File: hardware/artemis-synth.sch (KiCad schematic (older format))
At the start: 41 parts, among them IC1 ATMEGA328P, J1 AVR-ISP-6, J2 CONN JACK STEREO R/A 3PIN 3.5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, SW1 SWITCH_PUSH_CW, SW10 SWITCH_PUSH_CW, SW2 SWITCH_PUSH_CW, SW3 SWITCH_PUSH_CW, SW4 SWITCH_PUSH_CW, SW5 SWITCH_PUSH_CW, SW6 SWITCH_PUSH_CW, SW7 SWITCH_PUSH_CW, SW8 SWITCH_PUSH_CW, SW9 SWITCH_PUSH_CW, U1 MCP4921

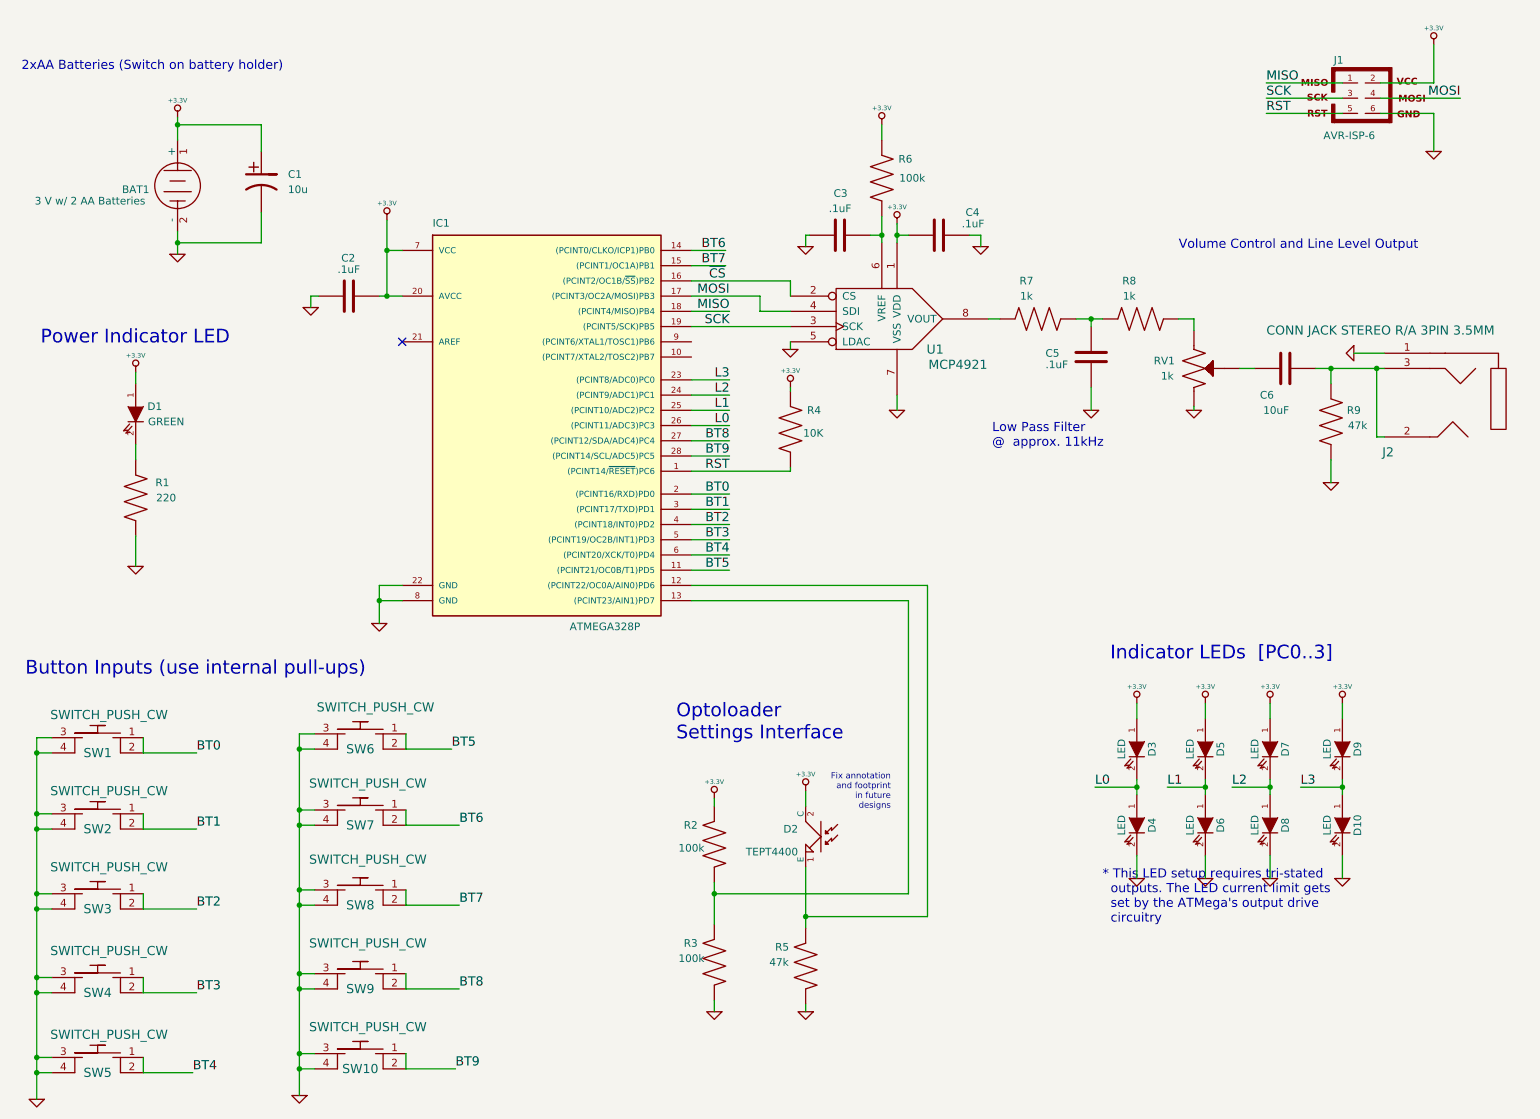
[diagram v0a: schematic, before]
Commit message: Generated latest gerber files for the v2rC board. Should be the final changes before getting sent out. Cleared todo list, plotted latest pdf of schematic. Changed output stage to add a pot which approximates a log pot (using R8). Changed C6 to move lower frequency pole up to 2Hz from .1Hz. Moved HF pole to about 5kHz to fit the new output samplign rate of 11kHz. Ideally we can mvoe back to 22kHz with some firmware optimization. THe new output stage is also boosted from its previous form in v2rB so that it can drive headphones pretty loudly.
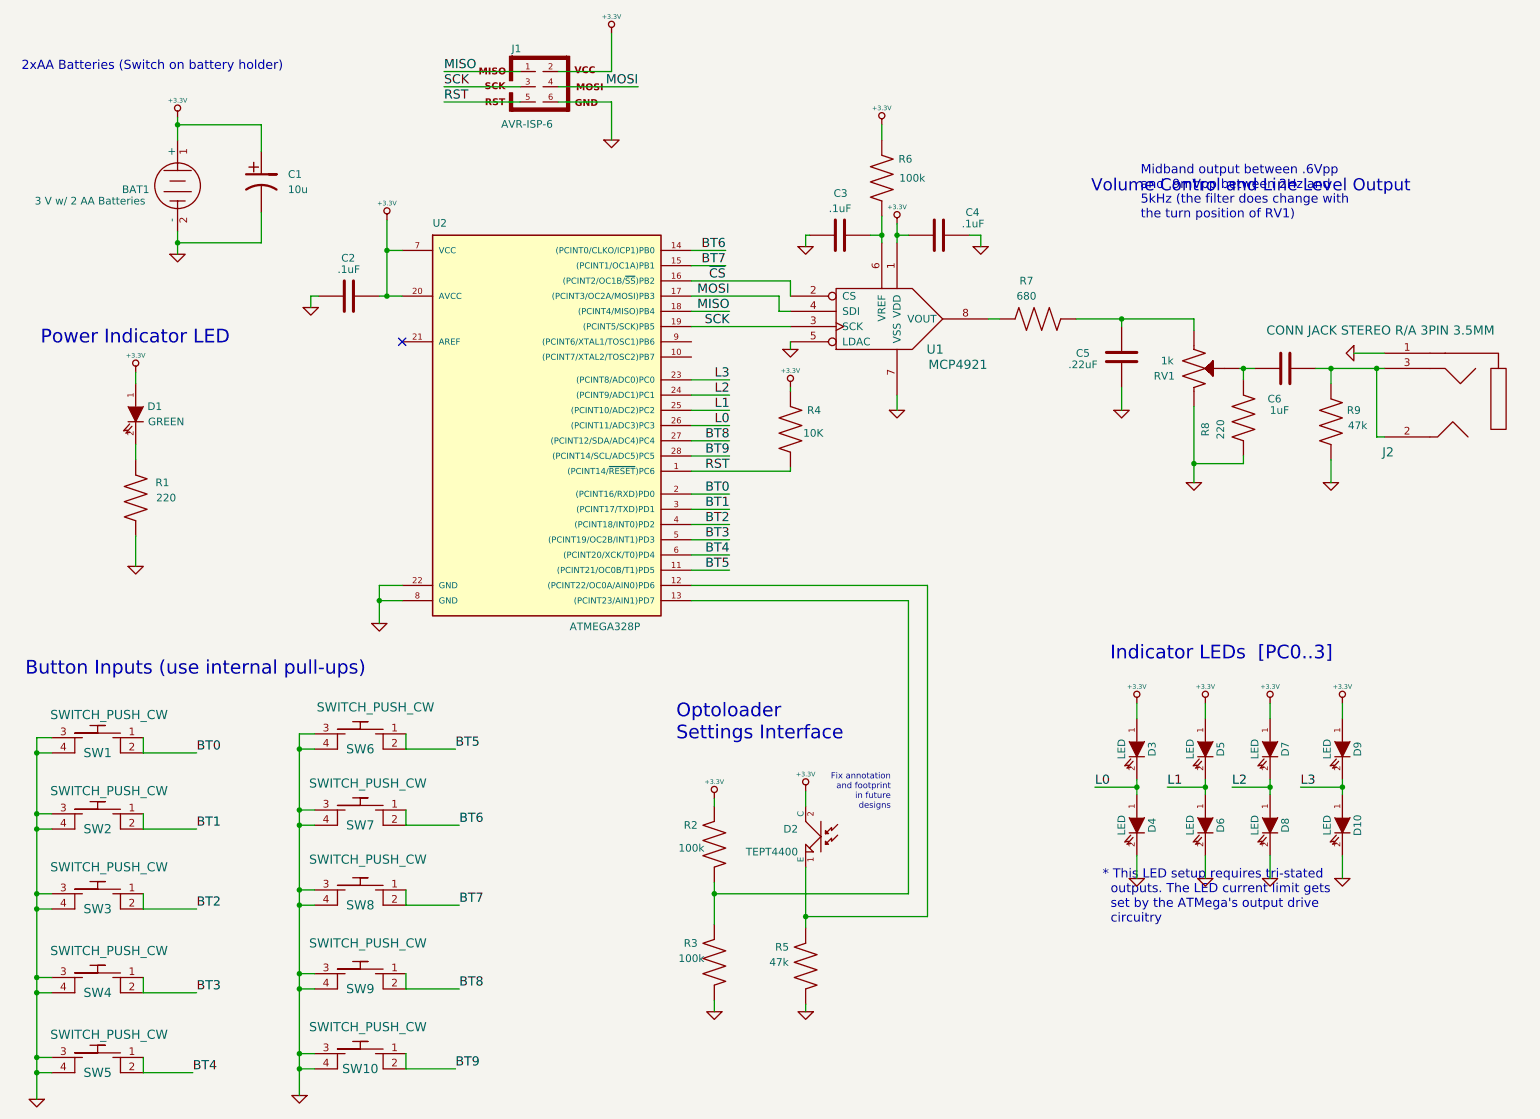
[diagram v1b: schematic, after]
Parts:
- C5: value .1uF -> .22uF
- C6: value 10uF -> 1uF; footprint C1V8 -> C1
- D1, D10, D2, D3, D4, D5, D6, D7, D8, D9: footprint LED-3MM -> LED-3MM-CORRECTED
- R7: value 1k -> 680
- R8: value 1k -> 220
- renumbered IC1 to U2
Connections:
- net GND: now also R8.1, RV1.1; no longer RV1.3
- net at C5.1, R7.2: now also RV1.3; no longer R8.1
- net at R8.2: now also C6.1, RV1.2; no longer RV1.1
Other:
- note added: "Midband output between .6Vpp \nand .9mVpp between 2Hz and \n5kHz (the filter does change with \nthe turn position of RV1)"
- note removed: "Low Pass Filter \n@ approx. 11kHz\n"
- moved on the sheet: C5, J1
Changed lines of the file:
@@
-EESchema Schematic File Version 2  date Tue 09 Jul 2013 12:50:36 PM EDT
+EESchema Schematic File Version 2  date Thu 11 Jul 2013 01:59:12 PM EDT
 LIBS:power
 LIBS:device
@@
 Sheet 1 1
 Title "Artemis Synthesizer"
-Date "9 jul 2013"
+Date "11 jul 2013"
 Rev "C"
 Comp "Christopher Woodall (c) 2012-2013"
@@
 F 0 "D4" H 8025 5950 50  0000 C CNN
 F 1 "LED" H 8025 5750 50  0000 C CNN
-F 2 "LED-3MM" H 8025 5850 50  0001 C CNN
+F 2 "LED-3MM-CORRECTED" H 8025 5850 50  0001 C CNN
 	1    8025 5850
 	0    1    1    0
@@
 F 0 "D6" H 8475 5950 50  0000 C CNN
 F 1 "LED" H 8475 5750 50  0000 C CNN
-F 2 "LED-3MM" H 8475 5850 50  0001 C CNN
+F 2 "LED-3MM-CORRECTED" H 8475 5850 50  0001 C CNN
 	1    8475 5850
 	0    1    1    0
@@
 F 0 "D8" H 8900 5950 50  0000 C CNN
 F 1 "LED" H 8900 5750 50  0000 C CNN
-F 2 "LED-3MM" H 8900 5850 50  0001 C CNN
+F 2 "LED-3MM-CORRECTED" H 8900 5850 50  0001 C CNN
 	1    8900 5850
 	0    1    1    0
@@
 F 0 "D10" H 9375 5950 50  0000 C CNN
 F 1 "LED" H 9375 5750 50  0000 C CNN
-F 2 "LED-3MM" H 9375 5850 50  0001 C CNN
+F 2 "LED-3MM-CORRECTED" H 9375 5850 50  0001 C CNN
 	1    9375 5850
 	0    1    1    0
@@
 F 0 "D9" H 9375 5450 50  0000 C CNN
 F 1 "LED" H 9375 5250 50  0000 C CNN
-F 2 "LED-3MM" H 9375 5350 50  0001 C CNN
+F 2 "LED-3MM-CORRECTED" H 9375 5350 50  0001 C CNN
 	1    9375 5350
 	0    1    1    0
@@
 F 0 "D7" H 8900 5450 50  0000 C CNN
 F 1 "LED" H 8900 5250 50  0000 C CNN
-F 2 "LED-3MM" H 8900 5350 50  0001 C CNN
+F 2 "LED-3MM-CORRECTED" H 8900 5350 50  0001 C CNN
 	1    8900 5350
 	0    1    1    0
@@
 F 0 "D5" H 8475 5450 50  0000 C CNN
 F 1 "LED" H 8475 5250 50  0000 C CNN
-F 2 "LED-3MM" H 8475 5350 50  0001 C CNN
+F 2 "LED-3MM-CORRECTED" H 8475 5350 50  0001 C CNN
 	1    8475 5350
 	0    1    1    0
@@
 F 0 "D3" H 8025 5450 50  0000 C CNN
 F 1 "LED" H 8025 5250 50  0000 C CNN
-F 2 "LED-3MM" H 8025 5350 50  0001 C CNN
+F 2 "LED-3MM-CORRECTED" H 8025 5350 50  0001 C CNN
 	1    8025 5350
 	0    1    1    0
@@
 	-1   0    0    -1
 $EndComp
-Text Label 3525 5350 0    60   ~ 0
+Text Label 3550 5350 0    60   ~ 0
 BT5
 Text Label 3575 5850 0    60   ~ 0
@@
 L +3.3V #PWR017
 U 1 1 4FE8EEAB
-P 9975 725
-F 0 "#PWR017" H 9975 685 30  0001 C CNN
-F 1 "+3.3V" H 9975 835 30  0000 C CNN
-	1    9975 725
+P 4575 650
+F 0 "#PWR017" H 4575 610 30  0001 C CNN
+F 1 "+3.3V" H 4575 760 30  0000 C CNN
+	1    4575 650
 	1    0    0    -1
 $EndComp
@@
 Text Label 5350 2575 2    60   ~ 0
 SCK
-Text Label 8875 1175 0    60   ~ 0
+Text Label 3475 1100 0    60   ~ 0
 RST
-Text Label 8875 1075 0    60   ~ 0
+Text Label 3475 1000 0    60   ~ 0
 SCK
-Text Label 8875 975  0    60   ~ 0
+Text Label 3475 900  0    60   ~ 0
 MISO
-Text Label 10150 1075 2    60   ~ 0
+Text Label 4750 1000 2    60   ~ 0
 MOSI
 $Comp
 L GND #PWR025
 U 1 1 4FDAC48B
-P 9975 1425
-F 0 "#PWR025" H 9975 1425 30  0001 C CNN
-F 1 "GND" H 9975 1355 30  0001 C CNN
-	1    9975 1425
-	1    0    0    -1
-$EndComp
-$Comp
-L ATMEGA328P-P IC1
+P 4575 1350
+F 0 "#PWR025" H 4575 1350 30  0001 C CNN
+F 1 "GND" H 4575 1280 30  0001 C CNN
+	1    4575 1350
+	1    0    0    -1
+$EndComp
+$Comp
+L ATMEGA328P-P U2
 U 1 1 4FDABFE3
 P 4100 3175
-F 0 "IC1" H 3400 4425 50  0000 L BNN
+F 0 "U2" H 3400 4425 50  0000 L BNN
 F 1 "ATMEGA328P" H 4300 1775 50  0000 L BNN
 F 2 "DIP-28__300" H 3500 1825 50  0001 C CNN
@@
 L AVR-ISP-6 J1
 U 1 1 4FDABF46
-P 9500 1075
-F 0 "J1" H 9350 1325 50  0000 C CNN
-F 1 "AVR-ISP-6" H 9250 800 50  0000 L BNN
-F 2 "pin_array_3x2" V 9000 1075 50  0001 C CNN
-	1    9500 1075
+P 4100 1000
+F 0 "J1" H 3950 1250 50  0000 C CNN
+F 1 "AVR-ISP-6" H 3850 725 50  0000 L BNN
+F 2 "pin_array_3x2" V 3600 1000 50  0001 C CNN
+	1    4100 1000
 	1    0    0    -1
 $EndComp
@@
 F 0 "D2" H 6100 5975 50  0000 L CNN
 F 1 "TEPT4400" H 6100 5825 50  0000 L CNN
-F 2 "LED-3MM" H 6100 5925 50  0001 C CNN
+F 2 "LED-3MM-CORRECTED" H 6100 5925 50  0001 C CNN
 	1    5950 5925
 	-1   0    0    -1
@@
 $EndComp
 $Comp
-L R_US R8
-U 1 1 51D3454A
-P 8050 2525
-F 0 "R8" V 8300 2600 50  0000 C CNN
-F 1 "1k" V 8200 2600 50  0000 C CNN
-F 2 "R4" V 8300 2600 50  0001 C CNN
-	1    8050 2525
-	0    -1   -1   0
-$EndComp
-$Comp
 L POT_US RV1
 U 1 1 51D34592
@@
 F 2 "THUMBWHEEL_POT_3352T" H 8225 2900 50  0001 C CNN
 	1    8400 2850
-	1    0    0    -1
+	1    0    0    1
 $EndComp
 $Comp
@@
 P 7375 2525
 F 0 "R7" V 7625 2600 50  0000 C CNN
-F 1 "1k" V 7525 2600 50  0000 C CNN
+F 1 "680" V 7525 2600 50  0000 C CNN
 F 2 "R4" V 7625 2600 50  0001 C CNN
 	1    7375 2525
@@
 L C C5
 U 1 1 51D3459E
-P 7725 2775
-F 0 "C5" H 7425 2800 50  0000 L CNN
-F 1 ".1uF" H 7425 2725 50  0000 L CNN
-F 2 "C1" H 7550 2775 50  0001 C CNN
-	1    7725 2775
+P 7925 2775
+F 0 "C5" H 7625 2800 50  0000 L CNN
+F 1 ".22uF" H 7575 2725 50  0000 L CNN
+F 2 "C1" H 7750 2775 50  0001 C CNN
+	1    7925 2775
 	1    0    0    -1
 $EndComp
@@
 U 1 1 51D345AA
 P 9000 2850
-F 0 "C6" V 8825 2925 50  0000 L CNN
-F 1 "10uF" V 8725 2825 50  0000 L CNN
-F 2 "C1V8" H 8825 2850 50  0001 C CNN
+F 0 "C6" V 8800 2875 50  0000 L CNN
+F 1 "1uF" V 8725 2825 50  0000 L CNN
+F 2 "C1" H 8825 2850 50  0001 C CNN
 	1    9000 2850
 	0    -1   -1   0
@@
 L GND #PWR030
 U 1 1 51D351B9
-P 8400 3125
-F 0 "#PWR030" H 8400 3125 30  0001 C CNN
-F 1 "GND" H 8400 3055 30  0001 C CNN
-	1    8400 3125
+P 8400 3600
+F 0 "#PWR030" H 8400 3600 30  0001 C CNN
+F 1 "GND" H 8400 3530 30  0001 C CNN
+	1    8400 3600
 	1    0    0    -1
 $EndComp
@@
 L GND #PWR031
 U 1 1 51D35725
-P 7725 3125
-F 0 "#PWR031" H 7725 3125 30  0001 C CNN
-F 1 "GND" H 7725 3055 30  0001 C CNN
-	1    7725 3125
+P 7925 3125
+F 0 "#PWR031" H 7925 3125 30  0001 C CNN
+F 1 "GND" H 7925 3055 30  0001 C CNN
+	1    7925 3125
 	1    0    0    -1
 $EndComp
@@
 F 0 "C1" H 2450 1675 50  0000 L CNN
 F 1 "10u" H 2450 1575 50  0000 L CNN
-F 2 "C1V8" H 2450 1675 50  0001 C CNN
+F 2 "C1V8" H 2650 1275 50  0001 C CNN
 	1    2275 1625
 	1    0    0    -1
@@
 F 0 "D1" V 1400 3275 50  0000 C CNN
 F 1 "GREEN" V 1500 3350 50  0000 C CNN
-F 2 "LED-3MM" V 1600 3350 50  0001 C CNN
+F 2 "LED-3MM-CORRECTED" V 1600 3350 50  0001 C CNN
 	1    1450 3150
 	0    1    1    0
@@
 Text Notes 7800 6500 0    60   ~ 0
 * This LED setup requires tri-stated\n  outputs. The LED current limit gets\n  set by the ATMega's output drive\n  circuitry
-Text Notes 7075 3375 0    60   ~ 0
-Low Pass Filter \n@  approx. 11kHz\n
-Text Notes 8300 2075 0    60   ~ 0
+Text Notes 8050 1875 0    60   ~ 0
+Midband output between .6Vpp \nand .9mVpp between 2Hz and \n5kHz (the filter does change with \nthe turn position of RV1)
+Text Notes 7725 1700 0    80   ~ 0
 Volume Control and Line Level Output
 Text Notes 825  2700 0    90   ~ 0
@@
 	-1   0    0    -1
 $EndComp
+$Comp
+L R_US R8
+U 1 1 51DECB38
+P 8725 3175
+F 0 "R8" V 8975 3250 50  0000 C CNN
+F 1 "220" V 8875 3250 50  0000 C CNN
+F 2 "R4" V 8975 3250 50  0001 C CNN
+	1    8725 3175
+	-1   0    0    1
+$EndComp
 Wire Wire Line
 	5750 3525 5100 3525
@@
 	3575 5850 3225 5850
 Wire Wire Line
-	3525 5350 3225 5350
+	3550 5350 3225 5350
 Wire Wire Line
 	3575 6375 3225 6375
@@
 	3050 4275 3050 4525
 Wire Wire Line
-	9625 1075 10150 1075
-Wire Wire Line
-	9975 975  9975 725
-Wire Wire Line
-	9625 975  9975 975
-Wire Wire Line
-	8875 1175 9375 1175
+	4225 1000 4750 1000
+Wire Wire Line
+	4575 900  4575 650
+Wire Wire Line
+	4225 900  4575 900
+Wire Wire Line
+	3475 1100 3975 1100
 Wire Wire Line
 	5100 2575 5750 2575
 Wire Wire Line
-	9375 975  8875 975
-Wire Wire Line
-	9375 1075 8875 1075
-Wire Wire Line
-	9625 1175 9975 1175
-Wire Wire Line
-	9975 1175 9975 1425
+	3975 900  3475 900
+Wire Wire Line
+	3975 1000 3475 1000
+Wire Wire Line
+	4225 1100 4575 1100
+Wire Wire Line
+	4575 1100 4575 1350
 Wire Wire Line
 	5350 2475 5100 2475
@@
 	5100 3125 5350 3125
 Wire Wire Line
-	5750 2475 5550 2475
-Wire Wire Line
-	5550 2475 5550 2375
-Wire Wire Line
-	5550 2375 5100 2375
+	5750 2475 5675 2475
+Wire Wire Line
+	5675 2475 5675 2375
+Wire Wire Line
+	5675 2375 5100 2375
 Wire Wire Line
 	5750 2375 5750 2375
@@
 	9450 2750 9650 2750
 Wire Wire Line
-	8800 2850 8700 2850
-Wire Wire Line
-	8400 3125 8400 3100
-Wire Wire Line
-	8400 2600 8400 2525
-Wire Wire Line
-	8400 2525 8300 2525
-Wire Wire Line
-	7625 2525 7800 2525
-Wire Wire Line
-	7725 2575 7725 2525
-Connection ~ 7725 2525
-Wire Wire Line
-	7725 2975 7725 3125
+	8700 2850 8800 2850
+Wire Wire Line
+	8400 3100 8400 3600
+Wire Wire Line
+	8400 2525 8400 2600
+Wire Wire Line
+	7925 2975 7925 3125
 Wire Wire Line
 	7050 2525 7125 2525
@@
 Wire Wire Line
 	5850 5625 5850 5725
+Wire Wire Line
+	7625 2525 8400 2525
+Wire Wire Line
+	7925 2575 7925 2525
+Connection ~ 7925 2525
+Wire Wire Line
+	8725 2925 8725 2850
+Connection ~ 8725 2850
+Wire Wire Line
+	8400 3475 8725 3475
+Wire Wire Line
+	8725 3475 8725 3425
+Connection ~ 8400 3475
 $EndSCHEMATC
